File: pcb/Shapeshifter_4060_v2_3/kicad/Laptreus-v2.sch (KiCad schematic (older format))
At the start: 152 parts, among them IC1 ATMEGA32U4, J1 HRO-TYPE-C-31-M-12, J2 ISP, SW1 TAB, SW10 O, SW11 P, SW12 BKSP, SW13 ESC, SW14 A, SW15 S, SW16 D, SW17 F/LOWER, SW18 G, SW19 H, SW2 Q, SW20 J/RAISE, SW21 K, SW22 L, SW23 ;, SW24 \", SW25 SHIFT, SW26 Z, SW27 X, SW28 C, SW29 V, SW3 W, SW30 B, SW31 N, SW32 M, SW33 ,, SW34 ., SW35 /, SW36 ENTER, SW37 HYPER, SW38 CTRL/GRV, SW39 ALT/TAB, SW4 E, SW40 CMD, SW41 SHIFT, SW42 BKSP/LIFT, SW43 ENTER/LIFT, SW44 SPACE, SW45 LEFT, SW46 DOWN, SW47 UP, SW48 RIGHT, SW5 R, SW6 T, SW7 Y, SW8 U, SW9 I, U1 MCP73831T-2ATI/OT, U2 SPX3819-3.3, U3 MDBT40, U6 USBLC6-2SC6, X1 JSTPH, X2 JSTPH, Y1 8MHz

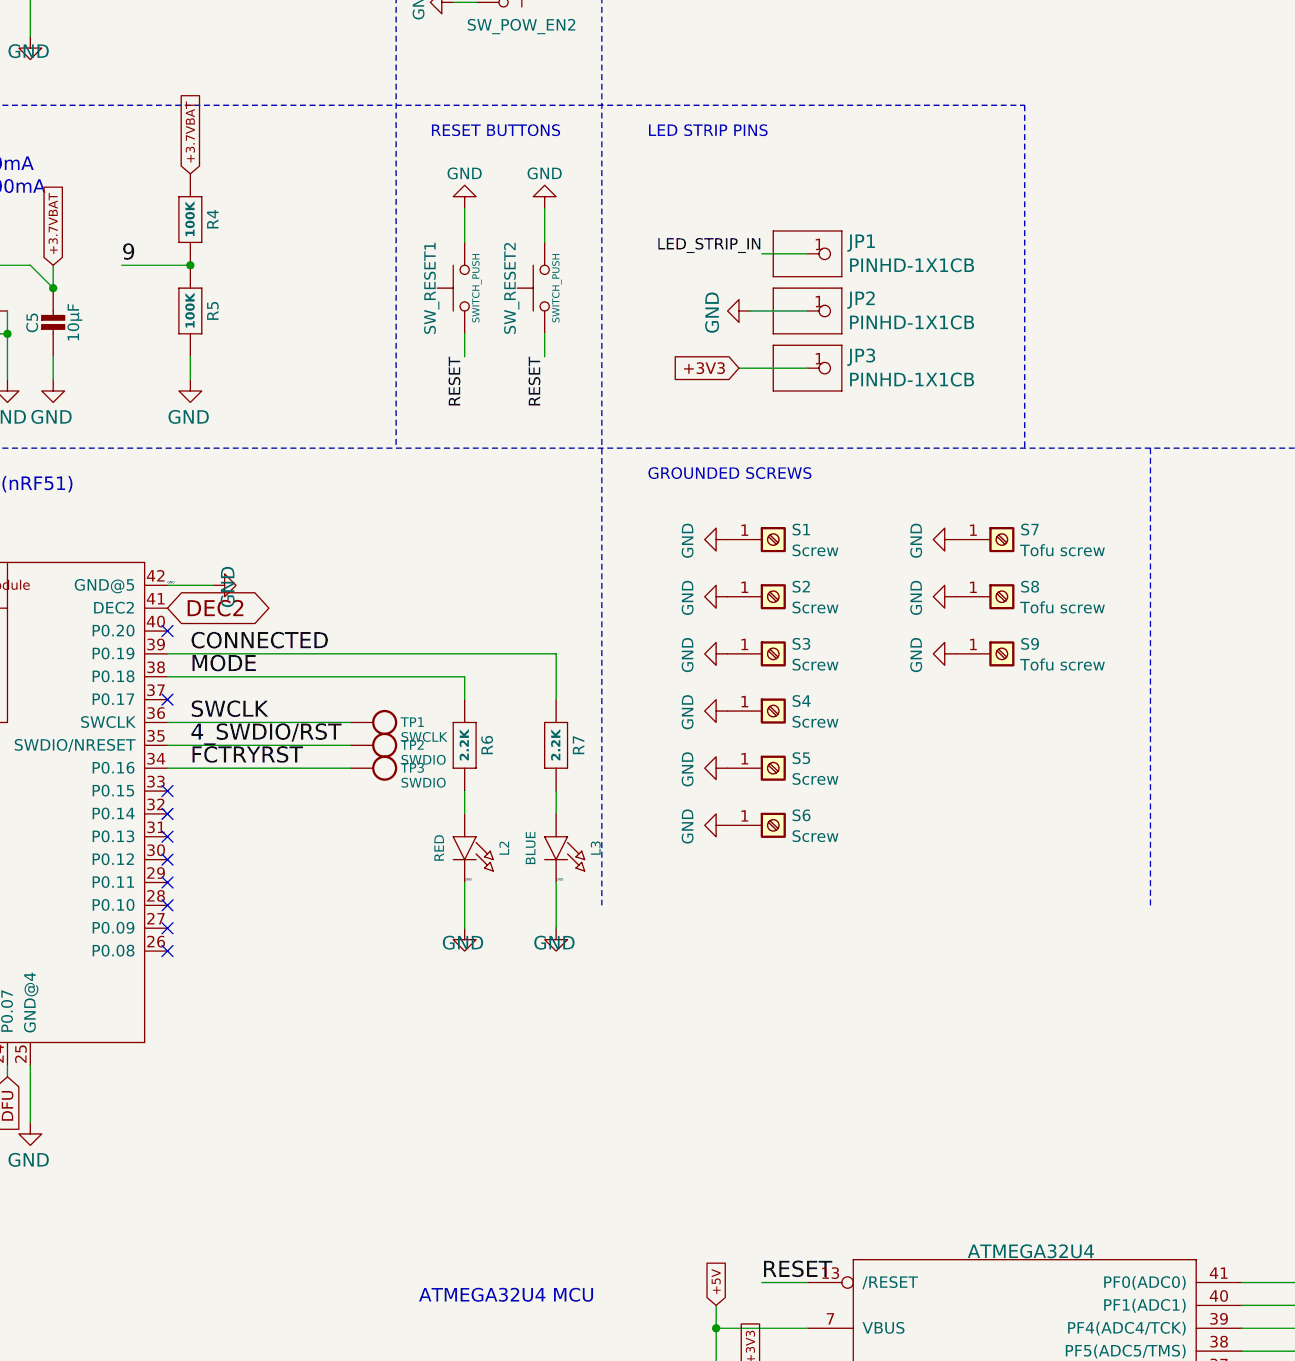
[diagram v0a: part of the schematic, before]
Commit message: update shapeshifter to use newer components from non-ble library, move mdbt40
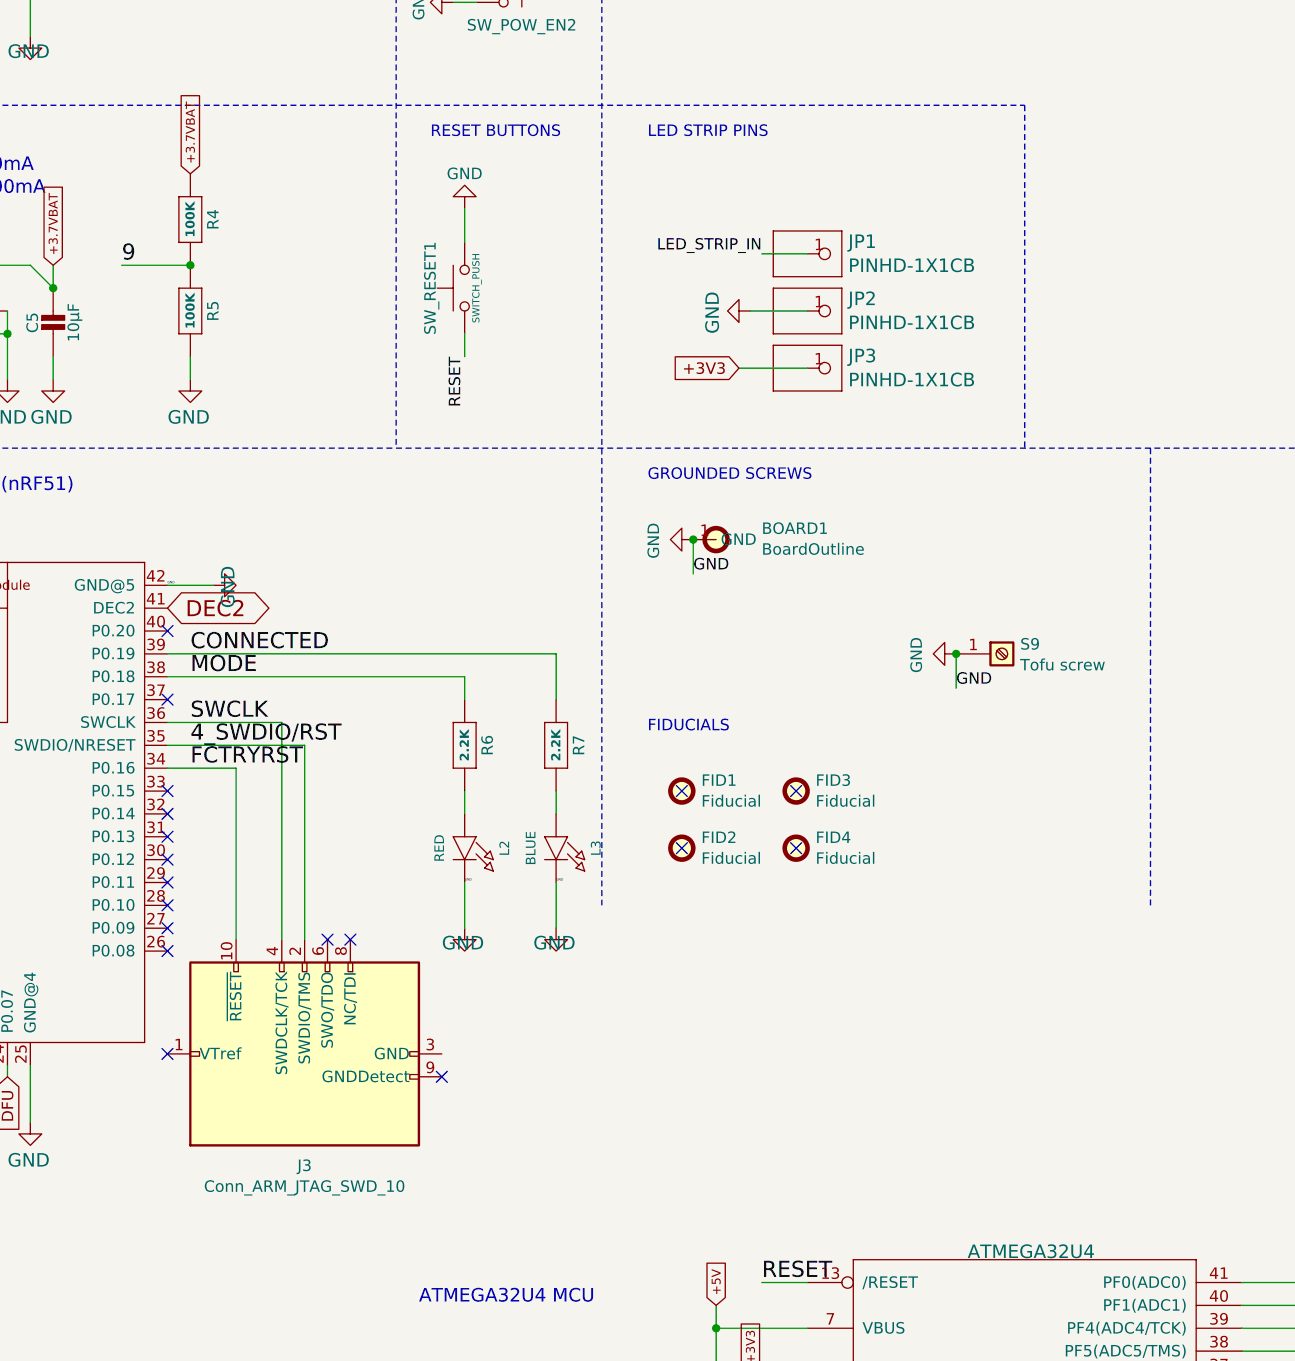
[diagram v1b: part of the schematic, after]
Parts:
- removed S1: Screw, Laptreus v2 Footprints:PKRH-Round, symbol Connector:Screw_Terminal_01x01
- removed S2, S3, S6: Screw, Laptreus v2 Footprints:PKRH, symbol Connector:Screw_Terminal_01x01
- removed S4, S5: Screw, Laptreus v2 Footprints:PKRHSL, symbol Connector:Screw_Terminal_01x01
- removed S7, S8: Tofu screw, Laptreus v2 Footprints:PKRH, symbol Connector:Screw_Terminal_01x01
- removed SW_RESET2: SWITCH_PUSH, Laptreus v2 Footprints:Hybrid_Kailh_MX_Socket_Through_Hole_No_Alignment_Pad, symbol Laptreus-v2:SW_Push
- removed TP1: SWCLK, Adafruit Feather 32u4 Bluefruit LE:PAD-1.5X2.0, symbol Adafruit-parts:TESTPOINT1.5X2.0MM_NOCREAM
- removed TP2, TP3: SWDIO, Adafruit Feather 32u4 Bluefruit LE:PAD-1.5X2.0, symbol Adafruit-parts:TESTPOINT1.5X2.0MM_NOCREAM
- added BOARD1: BoardOutline, Laptreus v2_2 Archive Footprints:60-percent-plus-tofu, symbol Laptreus-v2_2-archive:BoardOutline
- added FID1, FID2, FID3, FID4: Fiducial, Laptreus v2_2 Archive Footprints:FIDUCIAL, symbol Mechanical:Fiducial
- added J3: Conn_ARM_JTAG_SWD_10, Connector_PinHeader_1.27mm:PinHeader_2x05_P1.27mm_Vertical, symbol Connector:Conn_ARM_JTAG_SWD_10
- D1, D10, D11, D12, D13, D14, D15, D16, D17, D18, D19, D2, D20, D21, D22, D23, D24, D25, D26, D27, D28, D29, D3, D30, D31, D32, D33, D34, D35, D36, D37, D38, D39, D4, D40, D41, D42, D43, D44, D45, D46, D47, D48, D5, D6, D7, D8, D9: footprint Laptreus v2 Footprints:Diode-dual -> Laptreus v2_2 Archive Footprints:D_SOD-323_With_Adhesive
- F1: footprint Laptreus v2 Footprints:0805-NO -> Laptreus v2_2 Archive Footprints:Fuse_1812_4532Metric_With_Adhesive
- IC1: footprint Package_QFP:TQFP-44_10x10mm_P0.8mm -> Laptreus v2_2 Archive Footprints:TQFP-44_10x10mm_P0.8mm
- L1, L2, L3, L4: footprint Adafruit Feather 32u4 Bluefruit LE:CHIPLED_0805_NOOUTLINE -> Laptreus v2_2 Archive Footprints:LED_0603_1608Metric_Castellated_With_Adhesive
- R1, R10, R11, R12, R13, R2, R3, R4, R5, R6, R7, R8, R9: footprint Laptreus v2 Footprints:0805-NO -> Laptreus v2_2 Archive Footprints:R_0603_1608Metric_With_Adhesive
- SW1, SW10, SW11, SW13, SW15, SW16, SW17, SW18, SW19, SW2, SW20, SW21, SW22, SW26, SW27, SW28, SW29, SW3, SW30, SW31, SW32, SW33, SW34, SW35, SW37, SW38, SW39, SW4, SW40, SW41, SW42, SW43, SW44, SW45, SW46, SW47, SW48, SW5, SW6, SW7, SW8, SW9: footprint Laptreus v2 Footprints:Hybrid_Kailh_MX_Socket_Through_Hole_No_Alignment_Pad -> Laptreus v2_2 Archive Footprints:Hybrid_Kailh_MX_Choc_Socket_Through_Hole_With_Diode
- SW12: footprint Laptreus v2 Footprints:Hybrid_Kailh_MX_Socket -> Laptreus v2_2 Archive Footprints:Hybrid_Kailh_MX_Choc_Socket_Through_Hole_With_Diode
- SW14, SW23, SW24, SW25, SW36: footprint Laptreus v2 Footprints:Hybrid_Kailh_MX_Socket_Through_Hole_No_Alignment_Pad -> Laptreus v2_2 Archive Footprints:Hybrid_Kailh_MX_Choc_Socket_Through_Hole_With_Diode_No_Diode_Trace
- U1, U2: footprint Adafruit Feather 32u4 Bluefruit LE:SOT23-5 -> Laptreus v2_2 Archive Footprints:SOT-143_With_Adhesive
- X1, X2: footprint Adafruit Feather 32u4 Bluefruit LE:JSTPH2 -> Laptreus v2_2 Archive Footprints:JSTPH2-with-THT
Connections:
- net 4_SWDIO/RST: now also J3.2 (SWDIO/TMS)
- net FCTRYRST: now also J3.10 (~RESET~)
- net GND: now also BOARD1.1 (GND)
- net SWCLK: now also J3.4 (SWDCLK/TCK)
- new net: J3.3 (GND), J3.5 (GND)
- no-connect marks 26 -> 34
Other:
- note added: "FIDUCIALS"

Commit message: try to move all footprints into library. Need to do symbols still
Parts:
- removed J3: Conn_ARM_JTAG_SWD_10, Connector_PinHeader_1.27mm:PinHeader_2x05_P1.27mm_Vertical, symbol Connector:Conn_ARM_JTAG_SWD_10
- added U4: ARM-JTAG-SWD, Shapeshifter 4060 Footprints:ARM-JTAG-10-SWD-IDC, symbol ARM-JTAG-SWD:ARM-JTAG-SWD
- BOARD1: footprint Laptreus v2_2 Archive Footprints:60-percent-plus-tofu -> Shapeshifter 4060 Footprints:60_percent_plus_tofu_no_center_holes
- C1, C2, C20, C3, C4, C5, C6, C7: footprint Laptreus v2 Footprints:Capacitor-0805MP -> Shapeshifter 4060 Footprints:Capacitor_0805_MP
- D1, D10, D11, D12, D13, D14, D15, D16, D17, D18, D19, D2, D20, D21, D22, D23, D24, D25, D26, D27, D28, D29, D3, D30, D31, D32, D33, D34, D35, D36, D37, D38, D39, D4, D40, D41, D42, D43, D44, D45, D46, D47, D48, D5, D6, D7, D8, D9: footprint Laptreus v2_2 Archive Footprints:D_SOD-323_With_Adhesive -> Shapeshifter 4060 Footprints:D_SOD-323_With_Test_Points
- D49: footprint Adafruit Feather 32u4 Bluefruit LE:SOD-123 -> Shapeshifter 4060 Footprints:D_SOD-323_With_Test_Points
- F1: footprint Laptreus v2_2 Archive Footprints:Fuse_1812_4532Metric_With_Adhesive -> Shapeshifter 4060 Footprints:Fuse_1812_4532Metric
- FID1, FID2, FID3, FID4: footprint Laptreus v2_2 Archive Footprints:FIDUCIAL -> Shapeshifter 4060 Footprints:FIDUCIAL
- IC1: footprint Laptreus v2_2 Archive Footprints:TQFP-44_10x10mm_P0.8mm -> Shapeshifter 4060 Footprints:TQFP-44_10x10mm_P0.8mm
- J1: footprint Laptreus v2 Footprints:HRO-TYPE-C-31-M-12 -> Shapeshifter 4060 Footprints:HRO-TYPE-C-31-M-12
- J2: footprint Laptreus v2 Footprints:isp_standard -> Shapeshifter 4060 Footprints:ISP_Standard
- JP1, JP2, JP3: footprint Adafruit NeoPixel Ring 12:1X01-CLEANBIG -> Shapeshifter 4060 Footprints:1X01-CLEANBIG
- L1, L2, L3, L4: footprint Laptreus v2_2 Archive Footprints:LED_0603_1608Metric_Castellated_With_Adhesive -> Shapeshifter 4060 Footprints:LED_0603_1608Metric_Castellated
- R1, R10, R11, R12, R13, R2, R3, R4, R5, R6, R7, R8, R9: footprint Laptreus v2_2 Archive Footprints:R_0603_1608Metric_With_Adhesive -> Shapeshifter 4060 Footprints:R_0603_1608Metric
- S9: footprint Laptreus v2 Footprints:PKRH -> Shapeshifter 4060 Footprints:5mm_M2.5_Screw_Hole_Plated
- SW1, SW10, SW11, SW12, SW13, SW15, SW16, SW17, SW18, SW19, SW2, SW20, SW21, SW22, SW26, SW27, SW28, SW29, SW3, SW30, SW31, SW32, SW33, SW34, SW35, SW37, SW38, SW39, SW4, SW40, SW41, SW42, SW43, SW44, SW45, SW46, SW47, SW48, SW5, SW6, SW7, SW8, SW9: footprint Laptreus v2_2 Archive Footprints:Hybrid_Kailh_MX_Choc_Socket_Through_Hole_With_Diode -> Shapeshifter 4060 Footprints:Kailh_Socket_With_Diode
- SW14, SW23, SW24, SW25, SW36: footprint Laptreus v2_2 Archive Footprints:Hybrid_Kailh_MX_Choc_Socket_Through_Hole_With_Diode_No_Diode_Trace -> Shapeshifter 4060 Footprints:Kailh_Socket_With_Diode
- SW_POW_EN1, SW_POW_EN2: footprint Laptreus v2 Footprints:EG1218 -> Shapeshifter 4060 Footprints:EG1218
- SW_RESET1: footprint Laptreus v2 Footprints:SW_SPST_B3U-1000P -> Shapeshifter 4060 Footprints:SW_SPST_B3U-1000P
- U1, U2: footprint Laptreus v2_2 Archive Footprints:SOT-143_With_Adhesive -> Shapeshifter 4060 Footprints:SOT-23-5
- U3: footprint Adafruit Feather 32u4 Bluefruit LE:BLE_MODULE_RAYTAC_MDBT40 -> Shapeshifter 4060 Footprints:BLE_MODULE_RAYTAC_MDBT40
- U6: footprint Laptreus v2 Footprints:USBLC6-2SC6 -> Shapeshifter 4060 Footprints:SOT-23-6
- X1, X2: footprint Laptreus v2_2 Archive Footprints:JSTPH2-with-THT -> Shapeshifter 4060 Footprints:JSTPH2_With_THT
- Y1: footprint Adafruit Feather 32u4 Bluefruit LE:RESONATOR-SMD -> Shapeshifter 4060 Footprints:3_Pin_SMD_Resonator
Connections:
- net +5V: now also R1.2; no longer R1.1
- net 4_SWDIO/RST: now also U4.SWDIO
- net CHARGE: now also R1.1; no longer R1.2
- net COL0: now also D12.1 (K), D24.1 (K), D36.1 (K), D48.1 (K); no longer D12.2 (A), D24.2 (A), D36.2 (A), D48.2 (A)
- net COL1: now also D11.1 (K), D23.1 (K), D35.1 (K), D47.1 (K); no longer D11.2 (A), D23.2 (A), D35.2 (A), D47.2 (A)
- net COL10: now also D14.1 (K), D2.1 (K), D26.1 (K), D38.1 (K); no longer D14.2 (A), D2.2 (A), D26.2 (A), D38.2 (A)
- net COL11: now also D1.1 (K), D13.1 (K), D25.1 (K), D37.1 (K); no longer D1.2 (A), D13.2 (A), D25.2 (A), D37.2 (A)
- net COL2: now also D10.1 (K), D22.1 (K), D34.1 (K), D46.1 (K); no longer D10.2 (A), D22.2 (A), D34.2 (A), D46.2 (A)
- net COL3: now also D21.1 (K), D33.1 (K), D45.1 (K), D9.1 (K); no longer D21.2 (A), D33.2 (A), D45.2 (A), D9.2 (A)
- net COL4: now also D20.1 (K), D32.1 (K), D44.1 (K), D8.1 (K); no longer D20.2 (A), D32.2 (A), D44.2 (A), D8.2 (A)
- net COL5: now also D19.1 (K), D31.1 (K), D43.1 (K), D7.1 (K); no longer D19.2 (A), D31.2 (A), D43.2 (A), D7.2 (A)
- net COL6: now also D18.1 (K), D30.1 (K), D42.1 (K), D6.1 (K); no longer D18.2 (A), D30.2 (A), D42.2 (A), D6.2 (A)
- net COL7: now also D17.1 (K), D29.1 (K), D41.1 (K), D5.1 (K); no longer D17.2 (A), D29.2 (A), D41.2 (A), D5.2 (A)
- net COL8: now also D16.1 (K), D28.1 (K), D4.1 (K), D40.1 (K); no longer D16.2 (A), D28.2 (A), D4.2 (A), D40.2 (A)
- net COL9: now also D15.1 (K), D27.1 (K), D3.1 (K), D39.1 (K); no longer D15.2 (A), D27.2 (A), D3.2 (A), D39.2 (A)
- net CONNECTED: now also R7.2; no longer R7.1
- net FCTRYRST: now also U4.RESET
- net GND: now also U4.GND@1 (GND), U4.GND@2 (GND), U4.GND@3 (GND)
- net MODE: now also R6.2; no longer R6.1
- net SWCLK: now also U4.SWCLK
- net at L2.A: now also R6.1; no longer R6.2
- net at SW11.2: now also D11.2 (A); no longer D11.1 (K)
- net at SW23.2: now also D23.2 (A); no longer D23.1 (K)
- net at SW35.2: now also D35.2 (A); no longer D35.1 (K)
- net at SW47.2: now also D47.2 (A); no longer D47.1 (K)
- net at SW10.2: now also D10.2 (A); no longer D10.1 (K)
- net at SW22.2: now also D22.2 (A); no longer D22.1 (K)
- net at SW34.2: now also D34.2 (A); no longer D34.1 (K)
- net at SW46.2: now also D46.2 (A); no longer D46.1 (K)
- net at SW9.2: now also D9.2 (A); no longer D9.1 (K)
- net at SW21.2: now also D21.2 (A); no longer D21.1 (K)
- net at SW33.2: now also D33.2 (A); no longer D33.1 (K)
- net at SW45.2: now also D45.2 (A); no longer D45.1 (K)
- net at SW8.2: now also D8.2 (A); no longer D8.1 (K)
- net at SW20.2: now also D20.2 (A); no longer D20.1 (K)
- net at SW32.2: now also D32.2 (A); no longer D32.1 (K)
- net at SW44.2: now also D44.2 (A); no longer D44.1 (K)
- net at SW7.2: now also D7.2 (A); no longer D7.1 (K)
- net at SW19.2: now also D19.2 (A); no longer D19.1 (K)
- net at SW31.2: now also D31.2 (A); no longer D31.1 (K)
- net at SW43.2: now also D43.2 (A); no longer D43.1 (K)
- net at SW6.2: now also D6.2 (A); no longer D6.1 (K)
- net at SW18.2: now also D18.2 (A); no longer D18.1 (K)
- net at SW30.2: now also D30.2 (A); no longer D30.1 (K)
- net at SW42.2: now also D42.2 (A); no longer D42.1 (K)
- net at SW5.2: now also D5.2 (A); no longer D5.1 (K)
- net at SW17.2: now also D17.2 (A); no longer D17.1 (K)
- net at SW29.2: now also D29.2 (A); no longer D29.1 (K)
- net at SW41.2: now also D41.2 (A); no longer D41.1 (K)
- net at SW4.2: now also D4.2 (A); no longer D4.1 (K)
- net at SW16.2: now also D16.2 (A); no longer D16.1 (K)
- net at SW28.2: now also D28.2 (A); no longer D28.1 (K)
- net at SW40.2: now also D40.2 (A); no longer D40.1 (K)
- net at SW3.2: now also D3.2 (A); no longer D3.1 (K)
- net at SW15.2: now also D15.2 (A); no longer D15.1 (K)
- net at SW27.2: now also D27.2 (A); no longer D27.1 (K)
- net at SW39.2: now also D39.2 (A); no longer D39.1 (K)
- net at SW2.2: now also D2.2 (A); no longer D2.1 (K)
- net at SW14.2: now also D14.2 (A); no longer D14.1 (K)
- net at SW26.2: now also D26.2 (A); no longer D26.1 (K)
- net at SW38.2: now also D38.2 (A); no longer D38.1 (K)
- net at SW1.2: now also D1.2 (A); no longer D1.1 (K)
- net at SW13.2: now also D13.2 (A); no longer D13.1 (K)
- net at SW25.2: now also D25.2 (A); no longer D25.1 (K)
- net at SW37.2: now also D37.2 (A); no longer D37.1 (K)
- net at SW12.2: now also D12.2 (A); no longer D12.1 (K)
- net at SW24.2: now also D24.2 (A); no longer D24.1 (K)
- net at SW36.2: now also D36.2 (A); no longer D36.1 (K)
- net at SW48.2: now also D48.2 (A); no longer D48.1 (K)
- net at L3.A: now also R7.1; no longer R7.2
